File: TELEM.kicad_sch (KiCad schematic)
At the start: 11 parts, among them U5 TPS561208DDCR

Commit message: Update
Update
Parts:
- removed C1: 44muF, symbol Device:C_Small
- removed C2: 20.1muF, symbol Device:C_Small
- removed C3: 0.1 muF, symbol Device:C_Small
- removed FUSE_PWR1: 2A 12V PTC fuse, Fuse:Fuse_1812_4532Metric, symbol Device:Fuse
- removed L1: L_Small, symbol Device:L_Small
- removed R4, R6: 72.5, symbol Device:R_Small_US
- removed R5: 27.5, symbol Device:R_Small_US
- removed R7: 3.09k, symbol Device:R_Small_US
- removed SCREW_PWR1: Screw_Terminal_01x02, TerminalBlock_Phoenix:TerminalBlock_Phoenix_MKDS-1,5-2-5.08_1x02_P5.08mm_Horizontal, symbol Connector:Screw_Terminal_01x02
- removed U5: TPS561208DDCR, DDC0006A_N, symbol tpsbuckconv561208:TPS561208DDCR
- added C4: 100nf, symbol Device:C_Small
- added R1, R10, R11, R2, R3, R9: 10k, symbol Device:R_Small_US
- added R8: R_Shunt_US, symbol Device:R_Shunt_US
- added U4: INA228AIDGSR, VSSOP10_DGS_TEX, symbol INA228:INA228AIDGSR
- added U6: TMP1075NDRLR, SOT5X3-6_DRL_TEX, symbol tmpsensor:TMP1075NDRLR
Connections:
- net 3.3 V: now also C4.1, R1.2, R10.1, R11.2, R2.2, R3.2, R8.2, R9.1, U4.6 (VS), U6.5 (V+)
- net GND: now also C4.2, R8.3, U4.1 (A1), U4.2 (A0), U4.7 (GND), U6.2 (GND), U6.4 (A0)
- new net: R8.1, U4.10 (IN+), U4.8 (VBUS)
- new net: R8.4, U4.9 (IN-)
- new net PWR_ALERT: R1.1, U4.3 (ALERT)
- new net PWR_SCL: R3.1, U4.5 (SCL)
- new net PWR_SDA: R2.1, U4.4 (SDA)
- new net TMP_ALERT: R11.1, U6.3 (ALERT)
- new net TMP_SCL: R10.2, U6.1 (SCL)
- new net TMP_SDA: R9.2, U6.6 (SDA)

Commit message: Updated Schematic
Updated parts of todo list for schematic
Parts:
- removed U4: INA228AIDGSR, VSSOP10_DGS_TEX, symbol INA228:INA228AIDGSR
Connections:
- net 3.3 V: no longer R8.2
- net GND: no longer R8.3
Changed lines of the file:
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@@
-	)
-	(junction
-		(at 93.98 41.91)
-		(diameter 0)
-		(color 0 0 0 0)
 	)
 	(junction
@@
 		(property "Intersheetrefs" "${INTERSHEET_REFS}"
 			(at 142.6852 49.53 0)
-			(hide yes)
-			(show_name no)
-			(do_not_autoplace no)
-			(effects
-				(font
-					(size 1.27 1.27)
-				)
-				(justify left)
-			)
-		)
-	)
-	(global_label "3.3 V"
-		(shape input)
-		(at 154.94 38.1 0)
-		(fields_autoplaced yes)
-		(effects
-			(font
-				(size 1.27 1.27)
-			)
-			(justify left)
-		)
-		(property "Intersheetrefs" "${INTERSHEET_REFS}"
-			(at 163.0052 38.1 0)
 			(hide yes)
 			(show_name no)
@@
 					(unit 1)
 				)
-			)
-		)
-	)
-	(symbol
-		(lib_id "INA228:INA228AIDGSR")
-		(at 93.98 39.37 0)
-		(unit 1)
-		(body_style 1)
-		(exclude_from_sim no)
-		(in_bom yes)
-		(on_board yes)
-		(in_pos_files yes)
-		(dnp no)
-		(fields_autoplaced yes)
-		(property "Reference" "U4"
-			(at 114.3 29.21 0)
-			(show_name no)
-			(do_not_autoplace no)
-			(effects
-				(font
-					(size 1.524 1.524)
-				)
-			)
-		)
-		(property "Value" "INA228AIDGSR"
-			(at 114.3 31.75 0)
-			(show_name no)
-			(do_not_autoplace no)
-			(effects
-				(font
-					(size 1.524 1.524)
-				)
-			)
-		)
-		(property "Footprint" "VSSOP10_DGS_TEX"
-			(at 93.98 39.37 0)
-			(hide yes)
-			(show_name no)
-			(do_not_autoplace no)
-			(effects
-				(font
-					(size 1.27 1.27)
-					(italic yes)
-				)
-			)
-		)
-		(property "Datasheet" "https://www.ti.com/lit/gpn/ina228"
-			(at 93.98 39.37 0)
-			(hide yes)
-			(show_name no)
-			(do_not_autoplace no)
-			(effects
-				(font
-					(size 1.27 1.27)
-					(italic yes)
-				)
-			)
-		)
-		(property "Description" ""
-			(at 93.98 39.37 0)
-			(hide yes)
-			(show_name no)
-			(do_not_autoplace no)
-			(effects
-				(font
-					(size 1.27 1.27)
-				)
-			)
-		)
-		(pin "7"
-		)
-		(pin "4"
-		)
-		(pin "1"
-		)
-		(pin "3"
-		)
-		(pin "2"
-		)
-		(pin "5"
-		)
-		(pin "6"
-		)
-		(pin "8"
-		)
-		(pin "9"
-		)
-		(pin "10"
-		)
-		(instances
-			(project "X19-Float-Board"
-				(path "/00000000-0000-0000-0000-000060e6118b/5aacdb22-1c13-4dbb-a723-da6d6af85e48"
-					(reference "U4")
-					(unit 1)
-				)
-			)
-		)
-	)
-	(symbol
-		(lib_id "power:GND")
-		(at 154.94 43.18 0)
-		(unit 1)
-		(body_style 1)
-		(exclude_from_sim no)
-		(in_bom yes)
-		(on_board yes)
-		(in_pos_files yes)
-		(dnp no)
-		(fields_autoplaced yes)
-		(property "Reference" "#PWR026"
-			(at 154.94 49.53 0)
-			(hide yes)
-			(show_name no)
-			(do_not_autoplace no)
-			(effects
-				(font
-					(size 1.27 1.27)
-				)
-			)
-		)
-		(property "Value" "GND"
-			(at 154.94 48.26 0)
-			(show_name no)
-			(do_not_autoplace no)
-			(effects
-				(font
-					(size 1.27 1.27)
-				)
-			)
-		)
-		(property "Footprint" ""
-			(at 154.94 43.18 0)
-			(hide yes)
-			(show_name no)
-			(do_not_autoplace no)
-			(effects
-				(font
-					(size 1.27 1.27)
-				)
-			)
-		)
-		(property "Datasheet" ""
-			(at 154.94 43.18 0)
-			(hide yes)
-			(show_name no)
-			(do_not_autoplace no)
-			(effects
-				(font
-					(size 1.27 1.27)
-				)
-			)
-		)
-		(property "Description" "Power symbol creates a global label with name \"GND\" , ground"
-			(at 154.94 43.18 0)
-			(hide yes)
-			(show_name no)
-			(do_not_autoplace no)
-			(effects
-				(font
-					(size 1.27 1.27)
-				)
-			)
-		)
-		(pin "1"
-		)
-		(instances
-			(project "X19-Float-Board"
-				(path "/00000000-0000-0000-0000-000060e6118b/5aacdb22-1c13-4dbb-a723-da6d6af85e48"
-					(reference "#PWR026")
-					(unit 1)
-				)

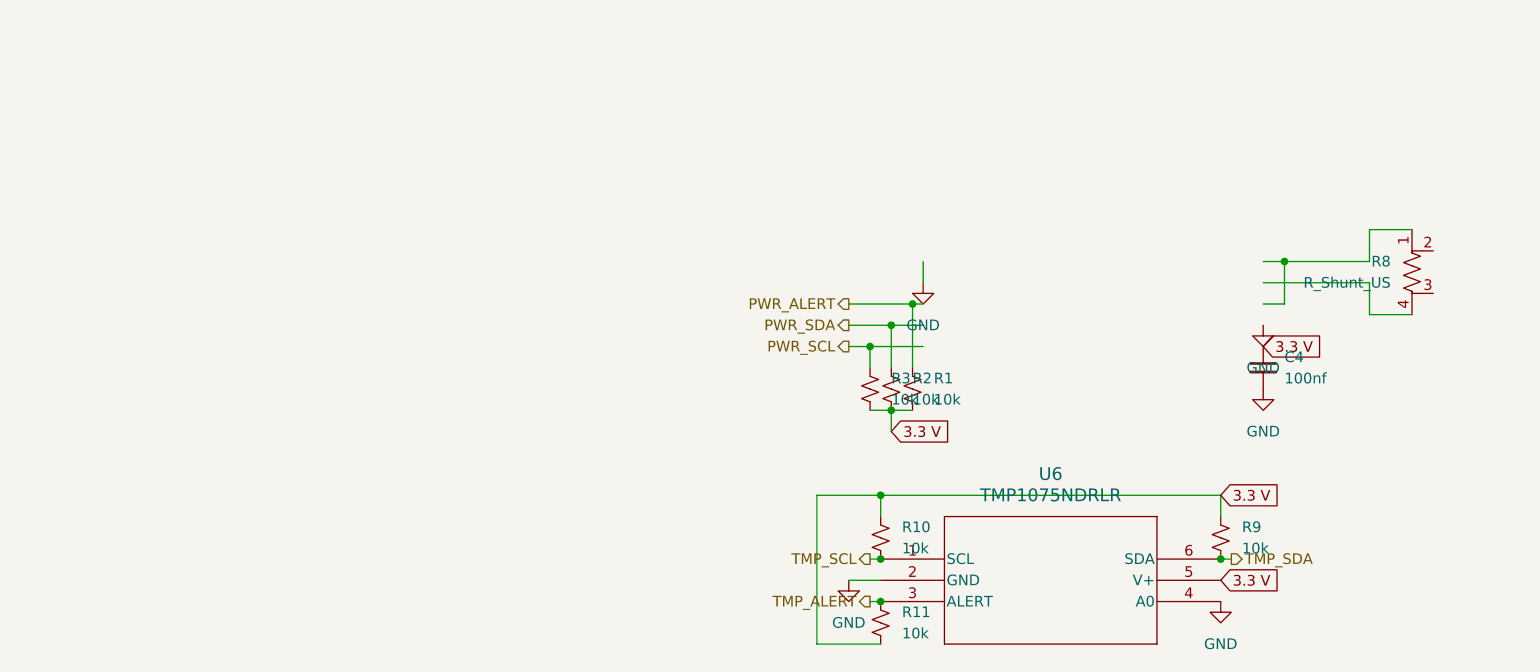
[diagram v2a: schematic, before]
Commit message: Updated Schematic
Updated schematic
Cleaned up dense portions
added H bridge
correct i2c wiring
added ferrite beads
added 12 V power monitoring
added stlink
added power mux
added power from usb
reformatted hierarichal sheets
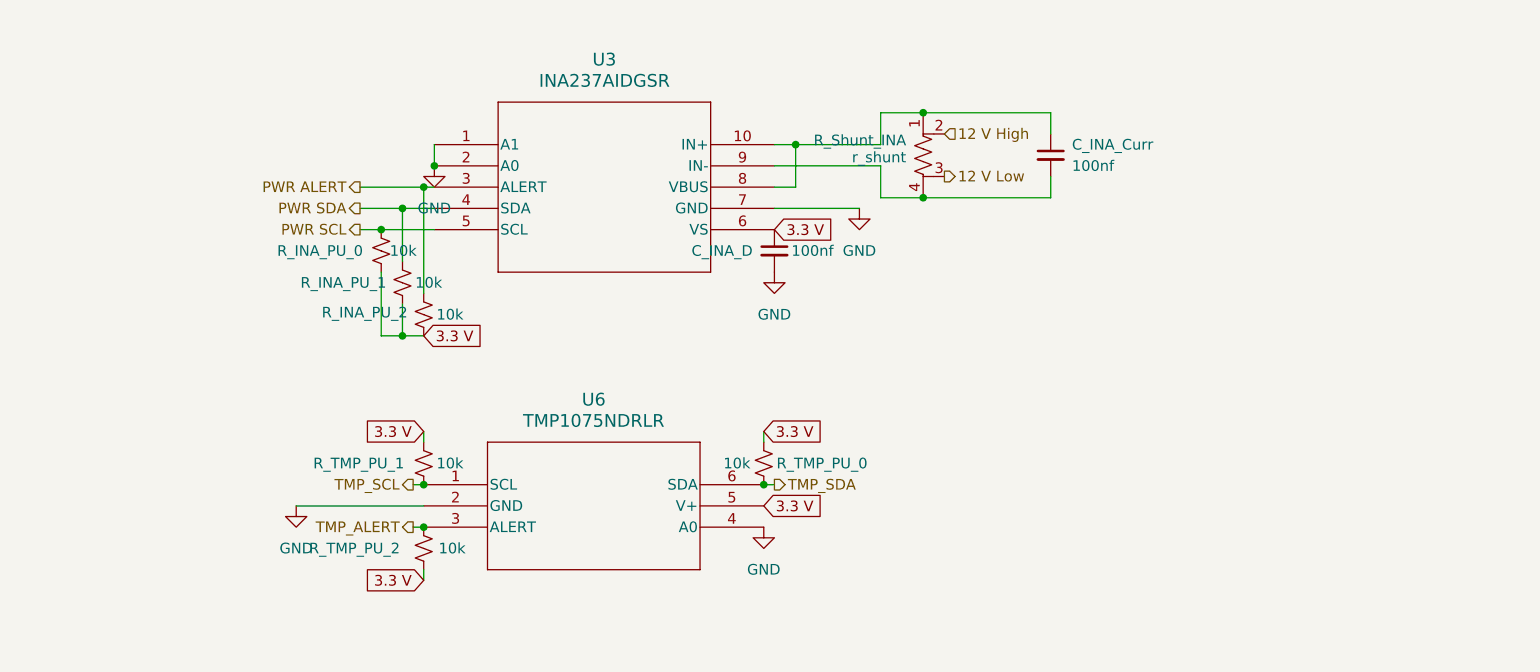
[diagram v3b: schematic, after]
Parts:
- added C_INA_Curr: 100nf, symbol Device:C_Small
- added U3: INA237AIDGSR, rov_sensors:VSSOP_IDGSR_TEX, symbol rov_sensors:INA237AIDGSR
- R_Shunt_INA: renamed from R8; value R_Shunt_US -> r_shunt
- renumbered C4 to C_INA_D, R3 to R_INA_PU_0, R2 to R_INA_PU_1, R1 to R_INA_PU_2, R9 to R_TMP_PU_0, R10 to R_TMP_PU_1, R11 to R_TMP_PU_2
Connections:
- net 3.3 V: now also U3.6 (VS)
- net GND: now also U3.1 (A1), U3.2 (A0), U3.7 (GND)
- net at R_Shunt_INA.1: now also C_INA_Curr.1, U3.10 (IN+), U3.8 (VBUS)
- net 12 V High: now reaches R_Shunt_INA.2
- net 12 V Low: now reaches R_Shunt_INA.3
- net at R_Shunt_INA.4: now also C_INA_Curr.2, U3.9 (IN-)
- net PWR_ALERT renamed PWR ALERT
- net PWR ALERT: now also U3.3 (ALERT)
- net PWR_SCL renamed PWR SCL
- net PWR SCL: now also U3.5 (SCL)
- net PWR_SDA renamed PWR SDA
- net PWR SDA: now also U3.4 (SDA)
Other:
- moved on the sheet: C_INA_D, R_INA_PU_0, R_INA_PU_1, R_INA_PU_2, R_Shunt_INA, R_TMP_PU_0, R_TMP_PU_1, R_TMP_PU_2, U6

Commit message: USB, TVS, LDO, Passives, I2C
applied changes to usb circuitry, tvs, ldo, passibes and i2c.
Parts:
- removed R_INA_PU_0, R_INA_PU_1, R_INA_PU_2, R_TMP_PU_0, R_TMP_PU_1, R_TMP_PU_2: 10k, symbol Device:R_Small_US

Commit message: float
float for claude review
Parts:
- R_Shunt_INA: value r_shunt -> 68 mΩ (adc range 0)
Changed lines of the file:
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@@
 			)
 		)
-		(property "Value" "r_shunt"
+		(property "Value" "68 mΩ (adc range 0)"
 			(at 91.948 26.924 0)
 			(show_name no)

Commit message: footprints
footprints
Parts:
- removed C_INA_Curr: 100nf, symbol Device:C_Small
- removed R_Shunt_INA: 68 mΩ (adc range 0), symbol Device:R_Shunt_US
- added R1: 1 mΩ, Resistor_SMD:R_2512_6332Metric_Pad1.40x3.35mm_HandSolder, symbol Device:R_US
- C_INA_D1: renamed from C_INA_D; footprint (none) -> Capacitor_SMD:C_0603_1608Metric_Pad1.08x0.95mm_HandSolder
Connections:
- net 12 V High: now also U3.10 (IN+), R1.1
- net 12 V Low: now also U3.8 (VBUS), U3.9 (IN-), R1.2

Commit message: Finished footprints
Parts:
- U6: footprint SOT5X3-6_DRL_TEX -> CustomFootprints:SOT5X3-6_DRL_TEX
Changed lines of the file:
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@@
 			)
 		)
-		(property "Footprint" "SOT5X3-6_DRL_TEX"
+		(property "Footprint" "CustomFootprints:SOT5X3-6_DRL_TEX"
 			(at 34.29 66.04 0)
 			(hide yes)
